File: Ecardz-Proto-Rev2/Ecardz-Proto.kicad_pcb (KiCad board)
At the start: 4 copper layers, 52.5 x 92 mm, 88 parts, among them IC1 M24LR04E-RMN6T/2, J1 Conn_01x02, J2 Conn_01x24, J3 Conn_01x06, J4 Conn_01x02, J5 Conn_01x02, Q1 NMOS, Q2 Q_PMOS_GSD, U1 STM32L071K8Ux

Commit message: second mech spin
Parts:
- removed C14, C22: TBD, parts-lib:C_2917
- removed the C23 at (474.0, 41.4)
- removed the C30 at (481.5, 41.4)
- added C23: 11mF, SamacSys_Parts:CPH3225A, F.Cu at (434.1, 6.58)
- added C23: 11mF, SamacSys_Parts:CPH3225A, F.Cu at (434.0, 17.8)
- added C23: 11mF, SamacSys_Parts:CPH3225A, F.Cu at (434.0, -4.12)
- added C26: 11mF, SamacSys_Parts:CPH3225A, F.Cu at (434.0, 14.1)
- added C26: 11mF, SamacSys_Parts:CPH3225A, F.Cu at (434.1, 2.83)
- added C30: 11mF, SamacSys_Parts:CPH3225A, F.Cu at (442.8, -2.25)
- added C30: 11mF, SamacSys_Parts:CPH3225A, F.Cu at (434.0, 10.3)
- added C30: 11mF, SamacSys_Parts:CPH3225A, F.Cu at (434.1, -0.92)
- moved J1 74.5 mm to (446.2, -10.2)
- moved J4 65.0 mm to (454.3, -6.98), turned to 90 degrees
- moved GND 64.9 mm to (446.2, -5.26), turned to 90 degrees
- moved VDD 64.9 mm to (448.8, -5.26), turned to 90 degrees
- moved C10 63.6 mm to (455.5, -2.72), turned to 0 degrees
- moved R10 63.5 mm to (455.5, -4.32), turned to 180 degrees
- moved TP9 62.1 mm to (457.4, 7.15)
- moved C12 61.3 mm to (455.5, -0.97), turned to 0 degrees
- moved R6 59.1 mm to (453.5, 3.26), turned to 0 degrees
- moved R25 58.6 mm to (452.7, 0.60), turned to 90 degrees
- moved C26 58.3 mm to (439.1, -2.24)
- moved R5 55.7 mm to (453.5, 5.01), turned to 0 degrees
- moved D4 54.5 mm to (456.2, 1.10), turned to 0 degrees
- moved C24 53.7 mm to (449.6, 3.07)
- moved C28 53.7 mm to (442.1, 3.07)
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- renumbered TP8 to GND, TP4 to VDD
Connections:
- J1 pad 1: VDD -> GND
- J1 pad 2: GND -> VDD
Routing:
- net /EINK/VCL: track 3.71 -> 24.2 mm, vias 1 -> 2
- net /EINK/GDR: track 31.4 -> 21.4 mm
- net /EINK/RESE: track 27.5 -> 21.0 mm
- net /EINK/VGL: track 17.9 -> 13.3 mm
- net /EINK/CS#: track 14.6 -> 11.6 mm
- net /EINK/SCL: track 8.71 -> 6.28 mm
- net /EINK/VGH: track 24.5 -> 22.6 mm
- net /EINK/SDA: track 13.4 -> 11.7 mm
- net GND: vias 21 -> 28
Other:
- board text added: "E-Card Rev 1 Avi Cahoon Isabella Schneider"

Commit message: all tracks connected
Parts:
- added C26: 11mF, SamacSys_Parts:CPH3225A, F.Cu at (438.7, -4.44)
- added C30: 11mF, SamacSys_Parts:CPH3225A, F.Cu at (434.9, -4.43)
- moved C28 19.4 mm to (435.5, -15.1), turned to 90 degrees
- moved C24 19.4 mm to (443.0, -15.1), turned to 90 degrees
- moved C29 18.3 mm to (446.8, -15.2), turned to 90 degrees
- moved C33 18.2 mm to (439.3, -15.1), turned to 90 degrees
- moved D4 17.6 mm to (452.6, -16.1)
- moved R25 16.2 mm to (449.3, -15.2)
- moved R3 14.0 mm to (462.7, 8.90)
- moved C9 12.4 mm to (460.0, 9.60), turned to 90 degrees
- moved C10 11.9 mm to (451.8, -14.0)
- moved C12 11.9 mm to (451.8, -12.2)
- moved C30 11.0 mm to (434.9, -9.84), turned to -90 degrees
- moved R2 10.7 mm to (462.7, 10.5)
- moved C21 9.23 mm to (450.2, 15.6), turned to 180 degrees
- moved J5 9.21 mm to (448.0, 1.10), turned to -90 degrees
- moved C23 8.86 mm to (430.7, -12.3), turned to 180 degrees
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- renumbered VDD to TP4, GND to TP8
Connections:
- C20 pad 1: Net-(C20-Pad1) -> /NFC/antenna
- C20 pad 2: GND -> /NFC/antenna
- C21 pad 1: Net-(C21-Pad1) -> /NFC/antenna
- C21 pad 2: GND -> /NFC/antenna
- IC1 pad 3: Net-(IC1-AC0) -> Net-(IC1-AC1)
- R18 pad 1: Net-(C21-Pad1) -> /NFC/antenna
- R18 pad 2: Net-(IC1-AC0) -> Net-(IC1-AC1)
- R19 pad 1: Net-(C20-Pad1) -> /NFC/antenna
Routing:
- net Net-(IC1-AC0): track 1107.8 -> 2.06 mm, vias 2 -> 0
- net (no net): track 0.00 -> 1044.0 mm
- net /NFC/antenna: track 0.00 -> 1003.9 mm, vias 0 -> 2
- net /NFC/NFC_POWER: track 0.00 -> 88.7 mm, vias 0 -> 1
- net /EINK/D/C#: track 17.5 -> 86.2 mm, vias 3 -> 2
- net /STM/I2C_NFC_SDA: track 4.90 -> 70.9 mm, vias 0 -> 2
- net /STM/NFC_BUSY: track 11.4 -> 77.3 mm, vias 0 -> 2
- net /EINK/CS#: track 11.6 -> 75.4 mm, vias 3 -> 2
- net /EINK/SCL: track 6.28 -> 69.2 mm
- net /STM/I2C_NFC_SCL: track 9.85 -> 70.2 mm, vias 0 -> 2
- net /EINK/SDA: track 11.7 -> 68.7 mm
- net /NFC/V_E_HARVEST: track 1.25 -> 54.8 mm, vias 1 -> 2
- net /EINK/EINK_POWER_CTRL_N: track 0.00 -> 48.7 mm, vias 0 -> 2
- net /EINK/BUSY: track 12.9 -> 58.1 mm
- net /EINK/RES#: track 16.7 -> 60.3 mm
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- added copper zone on F.Cu, net /NFC/V_E_HARVEST
- added copper zone on B.Cu, net GND
- added copper zone on F.Cu, net GND
- added copper zone on In1.Cu, net GND
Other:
- board text added: "GND VDD"

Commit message: final silkscreens
also made more space around antenna
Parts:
- moved TP9 3.04 mm to (456.5, 4.40)
- moved C23 0.41 mm to (430.7, 9.84)
- moved C23 0.41 mm to (430.7, -12.8)
- moved C24 0.41 mm to (443.0, -15.6)
- moved C25 0.41 mm to (429.5, 14.7)
- moved C26 0.41 mm to (438.7, -10.3)
- moved C26 0.41 mm to (430.7, 6.09)
- moved C27 0.41 mm to (437.0, 14.7)
- moved C28 0.41 mm to (435.5, -15.6)
- moved C29 0.41 mm to (446.8, -15.6)
- moved C30 0.41 mm to (434.9, -10.2)
- moved C30 0.41 mm to (430.7, 2.34)
- moved C30 0.41 mm to (430.8, -8.89)
- moved C30 0.41 mm to (434.9, -4.84)
- moved C31 0.41 mm to (440.7, 14.7)
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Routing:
- net (no net): track 1044.0 -> 0.00 mm
- net /STM/NFC_BUSY: track 77.3 -> 78.4 mm
- net /EINK/BUSY: track 58.1 -> 58.9 mm
- net /EINK/RES#: track 60.3 -> 61.1 mm
- net GND: vias 57 -> 73
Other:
- board text added: "3.3V"
- board text added: "BUSY"
- board text added: "CLK"
- board text added: "CS#"
- board text added: "D/C#"
- board text added: "DIO"
- board text added: "E-Card Rev 1 Dexter Siu Avi Cahoon Isabella Schneider"
- board text added: "GND"
- board text added: "NFC_BUSY"
- board text added: "RES#"
- board text added: "RST"
- board text added: "VDD"
- board text removed: "E-Card Rev 1 Avi Cahoon Isabella Schneider"
- board text removed: "GND VDD"

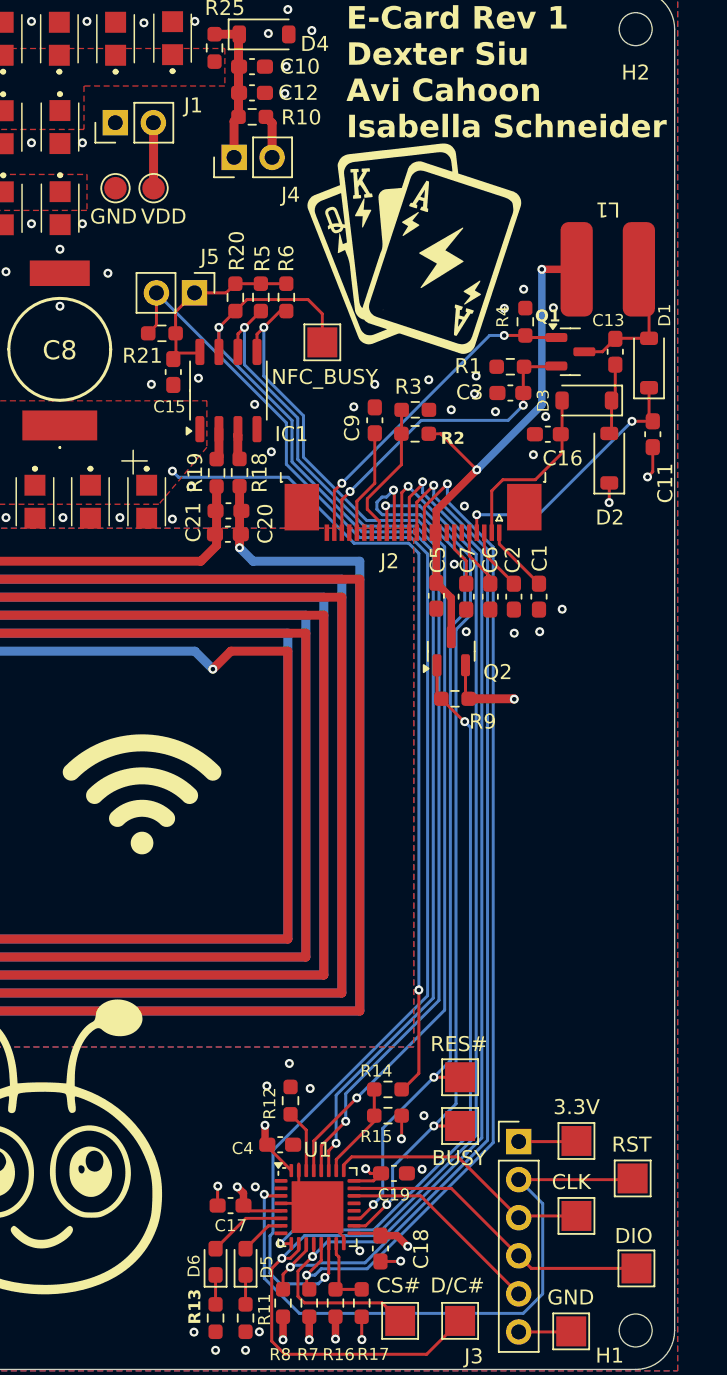
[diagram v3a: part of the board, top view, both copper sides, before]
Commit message: final fit check complete.
added updated step, wrl, gerbers and svg file used for silkscreen
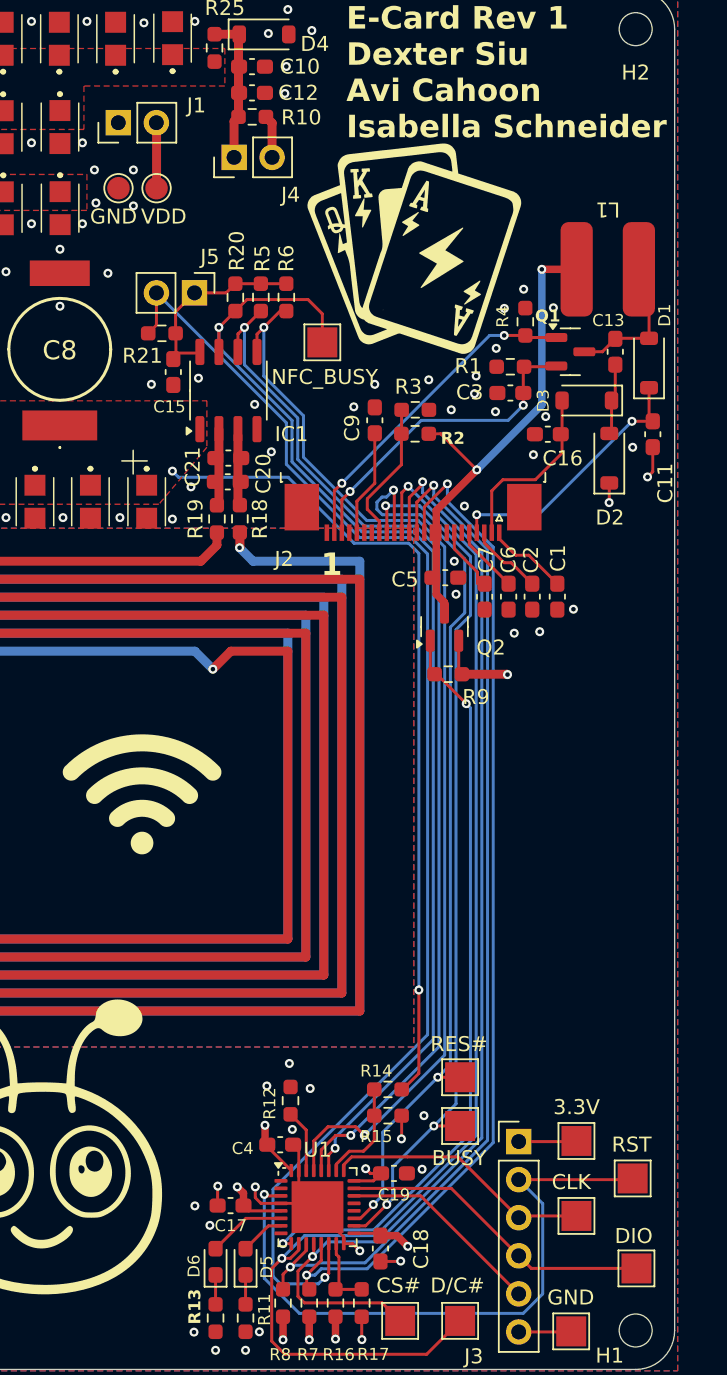
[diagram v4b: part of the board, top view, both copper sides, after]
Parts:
- moved C21 3.52 mm to (450.2, 12.1)
- moved C20 3.50 mm to (450.2, 13.7), turned to 180 degrees
- moved R18 3.08 mm to (451.0, 16.2)
- moved R19 3.08 mm to (449.5, 16.2)
- moved Q2 1.70 mm to (464.6, 23.4)
- moved R9 1.70 mm to (464.9, 26.5)
- moved C5 1.34 mm to (464.7, 20.1), turned to 0 degrees
- moved C1 1.23 mm to (472.2, 21.4)
- moved C2 1.23 mm to (470.5, 21.4)
- moved C6 1.23 mm to (468.9, 21.4)
- moved C7 1.22 mm to (467.3, 21.4)
- moved J1 0.20 mm to (442.9, -10.2)
- moved TP4 0.20 mm to (445.4, -5.88)
- moved TP8 0.20 mm to (442.9, -5.88)
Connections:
- C20 pad 1: /NFC/antenna -> Net-(IC1-AC1)
- C20 pad 2: /NFC/antenna -> Net-(IC1-AC0)
- C21 pad 1: /NFC/antenna -> Net-(IC1-AC1)
- C21 pad 2: /NFC/antenna -> Net-(IC1-AC0)
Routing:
- net /NFC/antenna: track 1003.9 -> 998.2 mm
- net GND: track 22.6 -> 27.9 mm, vias 73 -> 82
- net Net-(IC1-AC0): track 2.06 -> 5.19 mm
- net Net-(IC1-AC1): track 1.70 -> 4.71 mm
- net /STM/I2C_NFC_SDA: track 70.9 -> 73.1 mm
- net /EINK/EINK_POWER_CTRL_N: track 48.7 -> 50.4 mm
- net /EINK/VCL: track 35.8 -> 34.3 mm
- net /EINK/VCOM: track 4.50 -> 5.52 mm
- net /EINK/VSL: track 4.22 -> 5.01 mm
- net /STM/I2C_NFC_SCL: track 70.2 -> 70.8 mm
- net /STM/EH_MEAS: track 6.46 -> 7.02 mm
- net /EINK/VSH1: track 3.99 -> 4.49 mm

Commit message: final final mech spin
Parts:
- moved TP4 0.71 mm to (445.4, -6.59)
- moved TP8 0.71 mm to (442.9, -6.59)
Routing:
- net VDD: track 36.3 -> 35.6 mm
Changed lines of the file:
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@@
 	(footprint "TestPoint:TestPoint_Pad_D1.5mm"
 		(layer "F.Cu")
-		(at 445.442385 -5.881454 90)
+		(at 445.442385 -6.591454 90)
 		(descr "SMD pad as test Point, diameter 1.5mm")
 		(tags "test point SMD pad")
@@
 	(footprint "TestPoint:TestPoint_Pad_D1.5mm"
 		(layer "F.Cu")
-		(at 442.902385 -5.881454 90)
+		(at 442.902385 -6.591454 90)
 		(descr "SMD pad as test Point, diameter 1.5mm")
 		(tags "test point SMD pad")
@@
 	)
 	(via
-		(at 443.9 -4.7)
+		(at 444.1 -5.5)
 		(size 0.6)
 		(drill 0.3)
@@
 	)
 	(via
-		(at 443.9 -7.1)
+		(at 444.1 -7.8)
 		(size 0.6)
 		(drill 0.3)
@@
 	)
 	(via
-		(at 441.3 -7.1)
+		(at 441.7 -7.7)
 		(size 0.6)
 		(drill 0.3)
@@
 	)
 	(via
-		(at 441.4 -4.9)
+		(at 441.7 -5.5)
 		(size 0.6)
 		(drill 0.3)
@@
 	)
 	(segment
+		(start 445.442385 -6.591454)
+		(end 445.442385 -10.237615)
+		(width 0.6)
+		(layer "F.Cu")
+		(net 5)
+	)
+	(segment
 		(start 465.6 26.325)
 		(end 465.8125 26.5375)
@@
 		(layer "F.Cu")
 		(net 5)
-	)
-	(segment
-		(start 445.442385 -5.881454)
-		(end 445.442385 -10.237615)
-		(width 0.6)
-		(layer "F.Cu")
-		(net 5)
